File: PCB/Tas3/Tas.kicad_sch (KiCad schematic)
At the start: 28 parts, among them J1 Shelly 1, J2 Conn_01x07, J3 USB-C, U1 MD8942, U2 Barcode, U3 CH340X, U4 ZXGD3009E6, U5 ZXGD3009E6

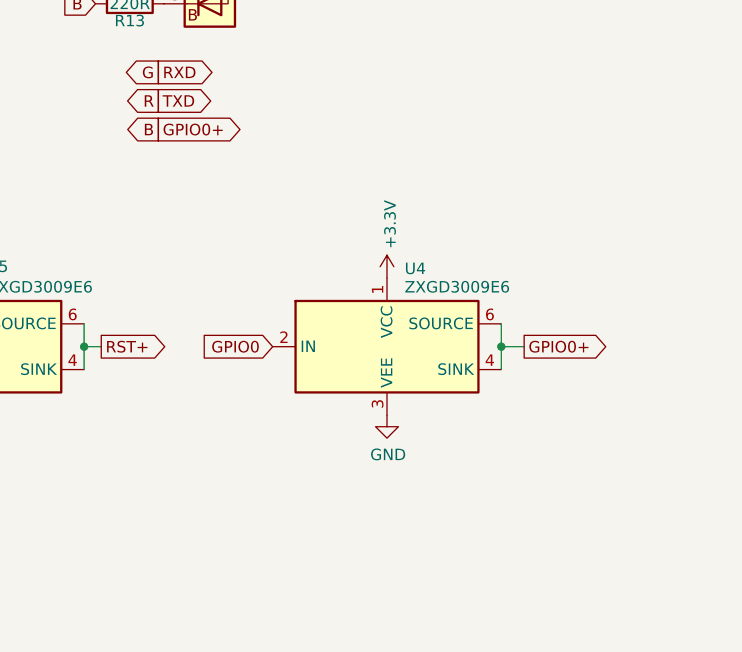
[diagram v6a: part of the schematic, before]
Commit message: GPIO buffer
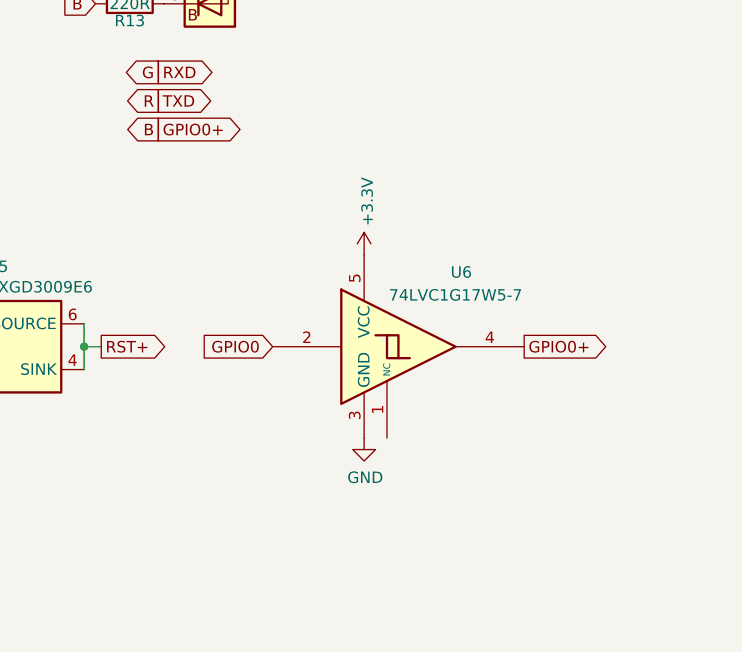
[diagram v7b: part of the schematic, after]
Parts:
- removed U4: ZXGD3009E6, RevK:SOT-23-6, symbol Driver_FET:ZXGD3009E6
- added U6: 74LVC1G17W5-7, RevK:SOT-25, symbol 74xGxx:74LVC1G17
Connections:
- net +3V3: now also U6.5 (VCC)
- net B: now also U6.4
- net GND: now also U6.3 (GND)
- net GPIO0: now also U6.2
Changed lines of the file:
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@@
   (junction (at 205.74 128.27) (diameter 0) (color 0 0 0 0)
-  )
-  (junction (at 252.095 128.27) (diameter 0) (color 0 0 0 0)
   )
   (junction (at 138.43 83.82) (diameter 0) (color 0 0 0 0)
@@
     (stroke (width 0) (type default))
   )
-  (wire (pts (xy 252.095 125.73) (xy 252.095 128.27))
-    (stroke (width 0) (type default))
-  )
   (wire (pts (xy 163.83 50.8) (xy 163.83 52.07))
     (stroke (width 0) (type default))
   )
-  (wire (pts (xy 254.635 128.27) (xy 252.095 128.27))
-    (stroke (width 0) (type default))
-  )
   (wire (pts (xy 153.67 53.34) (xy 156.21 53.34))
     (stroke (width 0) (type default))
   )
   (wire (pts (xy 205.74 128.27) (xy 207.645 128.27))
-    (stroke (width 0) (type default))
-  )
-  (wire (pts (xy 252.095 128.27) (xy 252.095 130.81))
     (stroke (width 0) (type default))
   )
@@
     )
   )
-  (symbol (lib_id "power:+3.3V") (at 239.395 120.65 0) (unit 1)
-    (in_bom yes) (on_board yes) (dnp no)
-    (property "Reference" "#PWR08" (at 239.395 124.46 0)
-      (effects (font (size 1.27 1.27)) hide)
-    )
-    (property "Value" "+3.3V" (at 239.776 117.3988 90)
-      (effects (font (size 1.27 1.27)) (justify left))
-    )
-    (property "Footprint" "" (at 239.395 120.65 0)
-      (effects (font (size 1.27 1.27)) hide)
-    )
-    (property "Datasheet" "" (at 239.395 120.65 0)
+  (symbol (lib_id "power:+3.3V") (at 236.855 118.11 0) (unit 1)
+    (in_bom yes) (on_board yes) (dnp no)
+    (property "Reference" "#PWR08" (at 236.855 121.92 0)
+      (effects (font (size 1.27 1.27)) hide)
+    )
+    (property "Value" "+3.3V" (at 237.236 114.8588 90)
+      (effects (font (size 1.27 1.27)) (justify left))
+    )
+    (property "Footprint" "" (at 236.855 118.11 0)
+      (effects (font (size 1.27 1.27)) hide)
+    )
+    (property "Datasheet" "" (at 236.855 118.11 0)
       (effects (font (size 1.27 1.27)) hide)
     )
@@
     )
   )
-  (symbol (lib_id "Driver_FET:ZXGD3009E6") (at 239.395 128.27 0) (unit 1)
-    (in_bom yes) (on_board yes) (dnp no) (fields_autoplaced)
-    (property "Reference" "U4" (at 241.3509 119.61 0)
-      (effects (font (size 1.27 1.27)) (justify left))
-    )
-    (property "Value" "ZXGD3009E6" (at 241.3509 121.658 0)
-      (effects (font (size 1.27 1.27)) (justify left))
-    )
-    (property "Footprint" "RevK:SOT-23-6" (at 239.395 140.97 0)
-      (effects (font (size 1.27 1.27)) hide)
-    )
-    (property "Datasheet" "https://www.diodes.com/assets/Datasheets/ZXGD3009E6.pdf" (at 230.505 121.92 0)
-      (effects (font (size 1.27 1.27)) hide)
-    )
-    (property "JLCPCB Rotation Offset" "180" (at 239.395 128.27 0)
-      (effects (font (size 1.27 1.27)) hide)
-    )
-    (pin "1")
-    (pin "2")
-    (pin "3")
-    (pin "4")
-    (pin "5")
-    (pin "6")
-    (instances
-      (project "Tas"
-        (path "/42713045-fffd-4b2d-ae1e-7232d705fb12"
-          (reference "U4") (unit 1)
-        )
-      )
-    )
-  )
-  (symbol (lib_id "power:GND") (at 239.395 135.89 0) (unit 1)
-    (in_bom yes) (on_board yes) (dnp no)
-    (property "Reference" "#PWR012" (at 239.395 142.24 0)
-      (effects (font (size 1.27 1.27)) hide)
-    )
-    (property "Value" "GND" (at 239.522 140.2842 0)
-      (effects (font (size 1.27 1.27)))
-    )
-    (property "Footprint" "" (at 239.395 135.89 0)
-      (effects (font (size 1.27 1.27)) hide)
-    )
-    (property "Datasheet" "" (at 239.395 135.89 0)
+  (symbol (lib_id "power:GND") (at 236.855 138.43 0) (unit 1)
+    (in_bom yes) (on_board yes) (dnp no)
+    (property "Reference" "#PWR012" (at 236.855 144.78 0)
+      (effects (font (size 1.27 1.27)) hide)
+    )
+    (property "Value" "GND" (at 236.982 142.8242 0)
+      (effects (font (size 1.27 1.27)))
+    )
+    (property "Footprint" "" (at 236.855 138.43 0)
+      (effects (font (size 1.27 1.27)) hide)
+    )
+    (property "Datasheet" "" (at 236.855 138.43 0)
       (effects (font (size 1.27 1.27)) hide)
     )
@@
         )
       )
+    )
+  )
+  (symbol (lib_id "74xGxx:74LVC1G17") (at 241.935 128.27 0) (unit 1)
+    (in_bom yes) (on_board yes) (dnp no)
+    (property "Reference" "U6" (at 247.65 120.015 0)
+      (effects (font (size 1.27 1.27)))
+    )
+    (property "Value" "74LVC1G17W5-7" (at 247.015 122.555 0)
+      (effects (font (size 1.27 1.27)))
+    )
+    (property "Footprint" "RevK:SOT-25" (at 239.395 128.27 0)
+      (effects (font (size 1.27 1.27)) hide)
+    )
+    (property "Datasheet" "https://www.ti.com/lit/ds/symlink/sn74lvc1g17.pdf" (at 241.935 128.27 0)
+      (effects (font (size 1.27 1.27)) hide)
+    )
+    (property "LCSC Part #" "C151394" (at 241.935 128.27 0)
+      (effects (font (size 1.27 1.27)) hide)
+    )
+    (property "JLCPCB Rotation Offset" "-90" (at 241.935 128.27 0)
+      (effects (font (size 1.27 1.27)) hide)
+    )
+    (pin "1")
+    (pin "2")
+    (pin "3")
+    (pin "4")
+    (pin "5")
+    (instances
+      (project "Tas"
+        (path "/42713045-fffd-4b2d-ae1e-7232d705fb12"
+          (reference "U6") (unit 1)
+        )
+      )

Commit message: Put back, as does not seem to save much
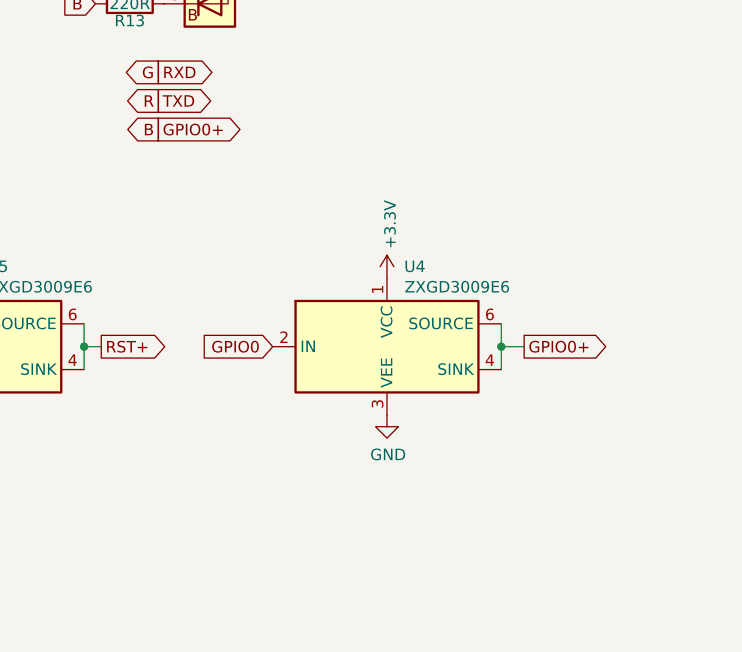
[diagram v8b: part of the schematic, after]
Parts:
- removed U6: 74LVC1G17W5-7, RevK:SOT-25, symbol 74xGxx:74LVC1G17
- added U4: ZXGD3009E6, RevK:SOT-23-6, symbol Driver_FET:ZXGD3009E6
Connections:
- net +3V3: now also U4.1 (VCC)
- net B: now also U4.4 (SINK), U4.6 (SOURCE)
- net GND: now also U4.3 (VEE)
- net GPIO0: now also U4.2 (IN)
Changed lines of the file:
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@@
   (junction (at 133.985 121.92) (diameter 0) (color 0 0 0 0)
+  )
+  (junction (at 252.095 128.27) (diameter 0) (color 0 0 0 0)
   )
   (junction (at 144.145 143.51) (diameter 0) (color 0 0 0 0)
@@
     (stroke (width 0) (type default))
   )
+  (wire (pts (xy 252.095 128.27) (xy 254.635 128.27))
+    (stroke (width 0) (type default))
+  )
   (wire (pts (xy 133.985 121.92) (xy 135.255 121.92))
     (stroke (width 0) (type default))
@@
     (stroke (width 0) (type default))
   )
+  (wire (pts (xy 252.095 125.73) (xy 252.095 128.27))
+    (stroke (width 0) (type default))
+  )
   (wire (pts (xy 132.715 121.92) (xy 133.985 121.92))
     (stroke (width 0) (type default))
@@
   )
   (wire (pts (xy 144.145 135.89) (xy 144.145 143.51))
+    (stroke (width 0) (type default))
+  )
+  (wire (pts (xy 252.095 128.27) (xy 252.095 130.81))
     (stroke (width 0) (type default))
   )
@@
     )
   )
-  (symbol (lib_id "power:+3.3V") (at 236.855 118.11 0) (unit 1)
-    (in_bom yes) (on_board yes) (dnp no)
-    (property "Reference" "#PWR08" (at 236.855 121.92 0)
-      (effects (font (size 1.27 1.27)) hide)
-    )
-    (property "Value" "+3.3V" (at 237.236 114.8588 90)
-      (effects (font (size 1.27 1.27)) (justify left))
-    )
-    (property "Footprint" "" (at 236.855 118.11 0)
-      (effects (font (size 1.27 1.27)) hide)
-    )
-    (property "Datasheet" "" (at 236.855 118.11 0)
+  (symbol (lib_id "power:+3.3V") (at 239.395 120.65 0) (unit 1)
+    (in_bom yes) (on_board yes) (dnp no)
+    (property "Reference" "#PWR08" (at 239.395 124.46 0)
+      (effects (font (size 1.27 1.27)) hide)
+    )
+    (property "Value" "+3.3V" (at 239.776 117.3988 90)
+      (effects (font (size 1.27 1.27)) (justify left))
+    )
+    (property "Footprint" "" (at 239.395 120.65 0)
+      (effects (font (size 1.27 1.27)) hide)
+    )
+    (property "Datasheet" "" (at 239.395 120.65 0)
       (effects (font (size 1.27 1.27)) hide)
     )
@@
     )
   )
-  (symbol (lib_id "power:GND") (at 236.855 138.43 0) (unit 1)
-    (in_bom yes) (on_board yes) (dnp no)
-    (property "Reference" "#PWR012" (at 236.855 144.78 0)
-      (effects (font (size 1.27 1.27)) hide)
-    )
-    (property "Value" "GND" (at 236.982 142.8242 0)
-      (effects (font (size 1.27 1.27)))
-    )
-    (property "Footprint" "" (at 236.855 138.43 0)
-      (effects (font (size 1.27 1.27)) hide)
-    )
-    (property "Datasheet" "" (at 236.855 138.43 0)
+  (symbol (lib_id "power:GND") (at 239.395 135.89 0) (unit 1)
+    (in_bom yes) (on_board yes) (dnp no)
+    (property "Reference" "#PWR012" (at 239.395 142.24 0)
+      (effects (font (size 1.27 1.27)) hide)
+    )
+    (property "Value" "GND" (at 239.522 140.2842 0)
+      (effects (font (size 1.27 1.27)))
+    )
+    (property "Footprint" "" (at 239.395 135.89 0)
+      (effects (font (size 1.27 1.27)) hide)
+    )
+    (property "Datasheet" "" (at 239.395 135.89 0)
       (effects (font (size 1.27 1.27)) hide)
     )
@@
         (path "/42713045-fffd-4b2d-ae1e-7232d705fb12"
           (reference "#PWR017") (unit 1)
+        )
+      )
+    )
+  )
+  (symbol (lib_id "Driver_FET:ZXGD3009E6") (at 239.395 128.27 0) (unit 1)
+    (in_bom yes) (on_board yes) (dnp no)
+    (property "Reference" "U4" (at 241.3 119.38 0)
+      (effects (font (size 1.27 1.27)) (justify left))
+    )
+    (property "Value" "ZXGD3009E6" (at 241.3509 121.658 0)
+      (effects (font (size 1.27 1.27)) (justify left))
+    )
+    (property "Footprint" "RevK:SOT-23-6" (at 239.395 140.97 0)
+      (effects (font (size 1.27 1.27)) hide)
+    )
+    (property "Datasheet" "https://www.diodes.com/assets/Datasheets/ZXGD3009E6.pdf" (at 230.505 121.92 0)
+      (effects (font (size 1.27 1.27)) hide)
+    )
+    (property "JLCPCB Rotation Offset" "180" (at 239.395 128.27 0)
+      (effects (font (size 1.27 1.27)) hide)
+    )
+    (pin "1")
+    (pin "2")
+    (pin "3")
+    (pin "4")
+    (pin "5")
+    (pin "6")
+    (instances
+      (project "Tas"
+        (path "/42713045-fffd-4b2d-ae1e-7232d705fb12"
+          (reference "U4") (unit 1)
         )
       )
@@
         )
       )
-    )
-  )
-  (symbol (lib_id "74xGxx:74LVC1G17") (at 241.935 128.27 0) (unit 1)
-    (in_bom yes) (on_board yes) (dnp no)
-    (property "Reference" "U6" (at 247.65 120.015 0)
-      (effects (font (size 1.27 1.27)))
-    )
-    (property "Value" "74LVC1G17W5-7" (at 247.015 122.555 0)
-      (effects (font (size 1.27 1.27)))
-    )
-    (property "Footprint" "RevK:SOT-25" (at 239.395 128.27 0)
-      (effects (font (size 1.27 1.27)) hide)
-    )
-    (property "Datasheet" "https://www.ti.com/lit/ds/symlink/sn74lvc1g17.pdf" (at 241.935 128.27 0)
-      (effects (font (size 1.27 1.27)) hide)
-    )
-    (property "LCSC Part #" "C151394" (at 241.935 128.27 0)
-      (effects (font (size 1.27 1.27)) hide)
-    )
-    (property "JLCPCB Rotation Offset" "-90" (at 241.935 128.27 0)
-      (effects (font (size 1.27 1.27)) hide)
-    )
-    (pin "1")
-    (pin "2")
-    (pin "3")
-    (pin "4")
-    (pin "5")
-    (instances
-      (project "Tas"
-        (path "/42713045-fffd-4b2d-ae1e-7232d705fb12"
-          (reference "U6") (unit 1)
-        )
-      )
